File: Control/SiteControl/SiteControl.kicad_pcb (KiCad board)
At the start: 2 copper layers, 109.2 x 48.3 mm, 149 parts, among them J1 RJ50, J2 CONN_01X03, J3 IDC_16Pin_Polarized, J4 CONN_01X06, J5 IDC-10_Polarized, J6 CONN_01X02, P1 Molex Minifit-JR 4.2mm, Q1 BC817-40, Q2 SI2323DDS-T1-GE3, U1 Opto_H11L1M, U10 LMV611, U11 MAX17552, U12 ICL3221, U13 Opto_H11L1M, U14 Opto_H11L1M, U15 12-Bit SPI ADC, U16 MCP7952, U17 74HCT125D,653, U18 SN74AUP1T87_Schmitt_XNOR, U2 Opto_H11L1M, U3 Opto_H11L1M, U4 Opto_H11L1M, U5 Opto_H11L1M, U6 PIC16LF1947, U7 SS_Relay_VO14642AT, U8 SS_Relay_VO14642AT, U9 LM43602, X1 CFS-20632768EZBB_32.768kHz, Y1 4MHz

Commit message: [Added] indicator LEDs and a new 3V3 Buck Converter to Site Control Board
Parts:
- removed the ? at (174.7, 98.6)
- removed the ? at (174.7, 100.0)
- removed the ? at (176.8, 104.4)
- removed the ? at (167.0, 98.9)
- removed the ? at (171.7, 99.5)
- removed the ? at (169.4, 98.5)
- removed the ? at (171.2, 98.5)
- added C47: 18pF/25V, Capacitors_SMD:C_0805, B.Cu at (182.9, 102.0)
- added C48: 100uF, Capacitors_SMD:C_1210, B.Cu at (186.4, 87.0)
- added C49: 0.1uF, Capacitors_SMD:C_0603, B.Cu at (183.9, 87.8)
- added D2: Reverse Polarity Error, LEDs:LED_0805, F.Cu at (173.9, 124.5)
- added D3: BATT Power, LEDs:LED_0805, F.Cu at (180.3, 123.5)
- added D4: 3V3 Power, LEDs:LED_0805, F.Cu at (184.2, 84.6)
- added D5: 5V Power, LEDs:LED_0805, F.Cu at (179.8, 84.5)
- added D6: RPi VSENSE, LEDs:LED_0805, F.Cu at (188.2, 84.4)
- added D7: RTC_MFP, LEDs:LED_0805, F.Cu at (182.0, 84.5)
- added D8: MCU Active, LEDs:LED_0805, F.Cu at (186.4, 84.5)
- added D9: MCU Mode, LEDs:LED_0805, F.Cu at (177.7, 84.4)
- added R53: 750R, Resistors_SMD:R_0603, F.Cu at (181.9, 88.0)
- added R54: 750R, Resistors_SMD:R_0603, F.Cu at (186.1, 87.6)
- added R55: 750R, Resistors_SMD:R_0603, F.Cu at (177.9, 87.8)
- added R56: 205K, Resistors_SMD:R_0805, B.Cu at (197.8, 99.5)
- added R57: 1M, Resistors_SMD:R_0805, B.Cu at (182.9, 100.0)
- added R58: 442K, Resistors_SMD:R_0805, B.Cu at (186.3, 102.0)
- C22: value 1uF/100V -> 47uF; footprint Capacitors_SMD:C_1206 -> Capacitors_SMD:c_elec_4x5.8
- C23: value 0.22uF -> 1uF; footprint Capacitors_SMD:C_0603 -> Capacitors_SMD:C_0805
- C24: value 10uF/6.3V -> 4.7uF; footprint Capacitors_SMD:C_1206 -> Capacitors_SMD:C_1210
- C25: value 0.47uF -> 2.2uF; footprint Capacitors_SMD:C_0603 -> Capacitors_SMD:C_0805
- C26: value 0.1uF -> 0.47uF; footprint Capacitors_SMD:C_0603 -> Capacitors_SMD:C_0805
- C36: value 0.47uF/50V -> 4.7uF; footprint Capacitors_SMD:C_0603 -> Capacitors_SMD:C_0805; moved to F.Cu
- C38, C41, C42, C43, C44, C45, C46, D1, R25, R26, R43, R49, R50, U15, U16, U17, U18: moved to B.Cu
- L2: value 150uH -> 22uH; footprint DigitalLogic:SRR7045-151M_Inductor -> Inductors:SELF-WE-PD-XXL; moved to B.Cu
- R32: value 191K -> 3K6; moved to F.Cu
- R33: value 49K9 -> 5K6; moved to F.Cu
- R34: value 158K -> 750R; moved to F.Cu
- R35: value 22R1 -> 1K6; moved to F.Cu
- R36: value 1K -> 750R; moved to F.Cu
- U11: value MAX17552 -> LM43602; footprint DigitalLogic:MAX17552 -> DigitalLogic:TI_HTSSOP-PWP-16
- moved C21 140.4 mm to (180.9, 150.2), turned to 90 degrees
- moved C18 134.1 mm to (177.6, 142.5), turned to 90 degrees
- moved R27 126.5 mm to (194.3, 138.0), turned to 180 degrees
- moved P1 125.2 mm to (153.4, 132.0)
- moved C37 124.7 mm to (194.9, 142.5), turned to 180 degrees
- moved R29 123.7 mm to (182.8, 136.0)
- moved R28 121.3 mm to (179.0, 138.0)
- moved C16 120.2 mm to (173.4, 142.3), turned to 90 degrees
- moved C38 119.5 mm to (193.9, 139.0), turned to 270 degrees
- moved C17 119.4 mm to (180.4, 142.0), turned to 90 degrees
- moved L1 119.1 mm to (191.4, 150.0), turned to 270 degrees
- moved C19 114.8 mm to (194.4, 140.0), turned to 180 degrees
- moved C20 106.2 mm to (183.4, 150.0), turned to 90 degrees
- moved C39 105.9 mm to (179.1, 136.0), turned to 180 degrees
- moved R25 103.3 mm to (192.1, 137.0), turned to 180 degrees
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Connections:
- net Net-(Q2-Pad3) renamed I1
- C23 pad 1: Net-(C23-Pad1) -> GND
- C23 pad 2: GND -> +BATT
- C24 pad 1: +3V3 -> GND
- C24 pad 2: GND -> +BATT
- C25 pad 1: +3V3 -> GND
- C25 pad 2: GND -> Net-(C25-Pad2)
- C26 pad 1: +3V3 -> Net-(C26-Pad1)
- C26 pad 2: GND -> Net-(C26-Pad2)
- C36 pad 1: +BATT -> GND
- C36 pad 2: GND -> +3V3
- L2 pad 1: Net-(L2-Pad1) -> Net-(C26-Pad2)
- R26 pad 1: GND -> RPi_5v_PGood
- R26 pad 2: RPi_5v_PGood -> +3V3
- R32 pad 1: Net-(R32-Pad1) -> Net-(D2-Pad2)
- R33 pad 1: Net-(R33-Pad1) -> Net-(D3-Pad1)
- R34 pad 1: +3V3 -> Net-(D4-Pad1)
- R34 pad 2: Net-(R33-Pad1) -> GND
- R35 pad 1: +3V3 -> Net-(D5-Pad1)
- R35 pad 2: Net-(C23-Pad1) -> GND
- R36 pad 1: Net-(R36-Pad1) -> Net-(D6-Pad1)
- R36 pad 2: +3V3 -> GND
- U11 pad 1: +BATT -> Net-(C26-Pad2)
- U11 pad 10: Net-(L2-Pad1) -> GND
- U11 pad 2: +BATT -> Net-(C26-Pad2)
- U11 pad 3: Net-(R32-Pad1) -> Net-(C26-Pad1)
- U11 pad 4: Net-(U11-Pad4) -> Net-(C25-Pad2)
- U11 pad 5: Net-(R33-Pad1) -> +3V3
- U11 pad 6: Net-(C23-Pad1) -> GND
- U11 pad 7: Net-(R36-Pad1) -> Net-(R56-Pad2)
- U11 pad 9: GND -> Net-(C47-Pad1)
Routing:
- net +5V: track 0.00 -> 48.7 mm, vias 0 -> 3
- net +3V3: track 8.07 -> 54.2 mm, vias 1 -> 3
- net GND: track 17.8 -> 43.1 mm, vias 0 -> 2
- net RPi_5V_En: track 0.00 -> 14.1 mm, vias 0 -> 1
- net INV_TOGGLE: track 30.6 -> 43.7 mm
- net INV_LCD_GND: track 90.0 -> 102.5 mm, vias 4 -> 6
- net INV_LED_PowerOn: track 28.0 -> 18.6 mm
- net INV_LCD_Data: track 24.6 -> 15.6 mm
- net INV_LED_OverTemp: track 35.4 -> 44.1 mm
- net RPi_5v_PGood: track 0.00 -> 8.61 mm, vias 0 -> 1
- net Net-(C39-Pad1): track 0.00 -> 7.54 mm
- net Net-(C37-Pad1): track 0.00 -> 7.10 mm
- net Net-(C26-Pad1): track 0.00 -> 7.03 mm
- net Net-(C47-Pad1): track 0.00 -> 6.58 mm
- net Net-(R56-Pad2): track 0.00 -> 3.94 mm
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- added copper zone on F.Cu, net +5V
- added copper zone on F.Cu, net +BATT
- added copper zone on F.Cu, net GND
- added copper zone on B.Cu, net Net-(C26-Pad2)
- added copper zone on F.Cu, net Net-(C37-Pad2)
- removed copper zone on F.Cu, net +3V3
- removed copper zone on B.Cu, net Net-(L2-Pad1)
- removed copper zone on F.Cu, net Net-(L2-Pad1)
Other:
- board size 109.2 x 48.3 mm -> 52.5 x 115.5 mm

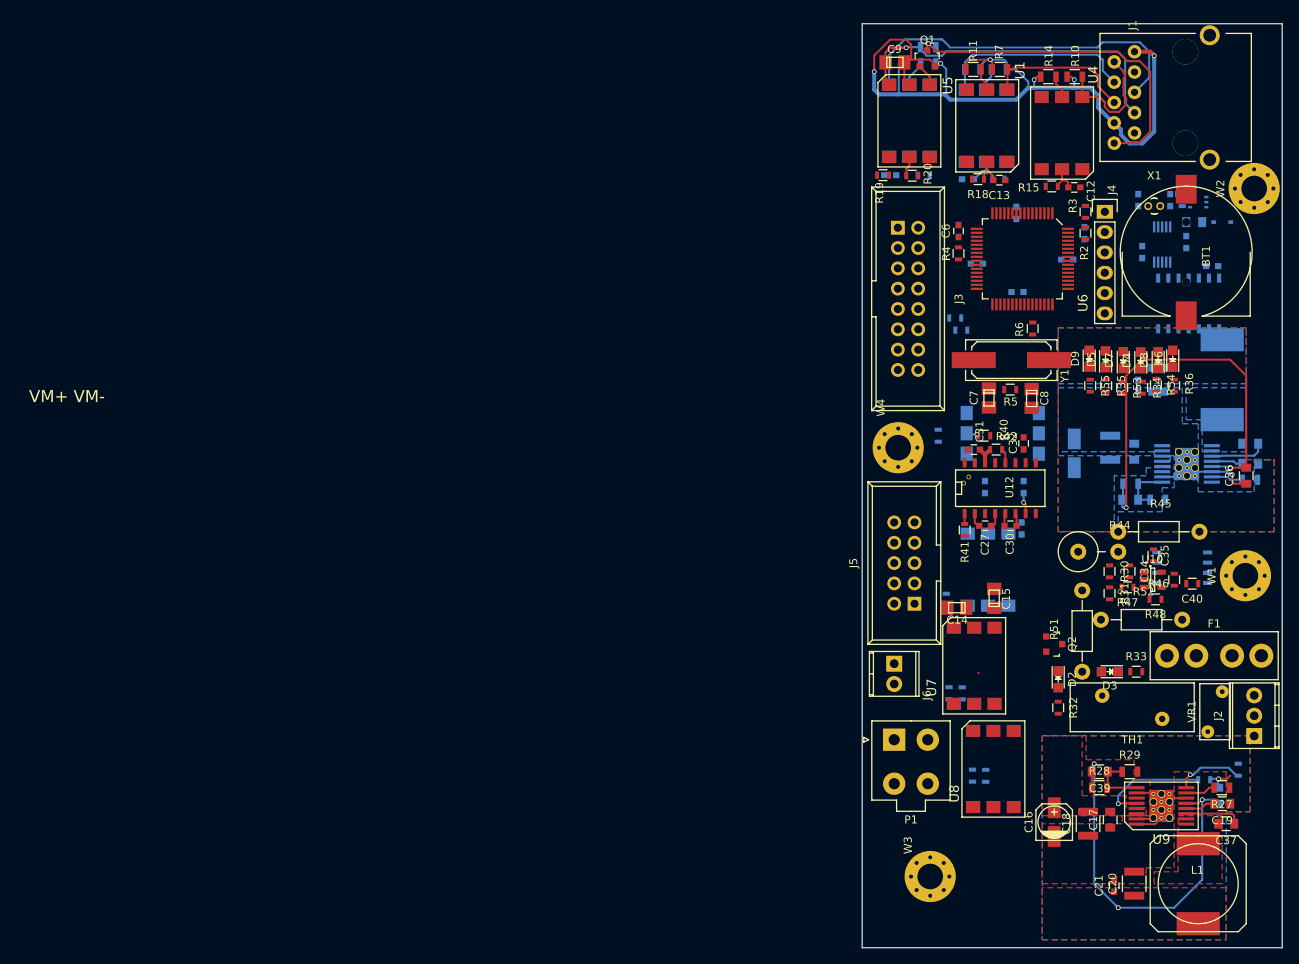
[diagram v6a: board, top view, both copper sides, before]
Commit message: [WIP] Preliminary routing and silkscreen placement for Rev B of Site Control Board Compelte
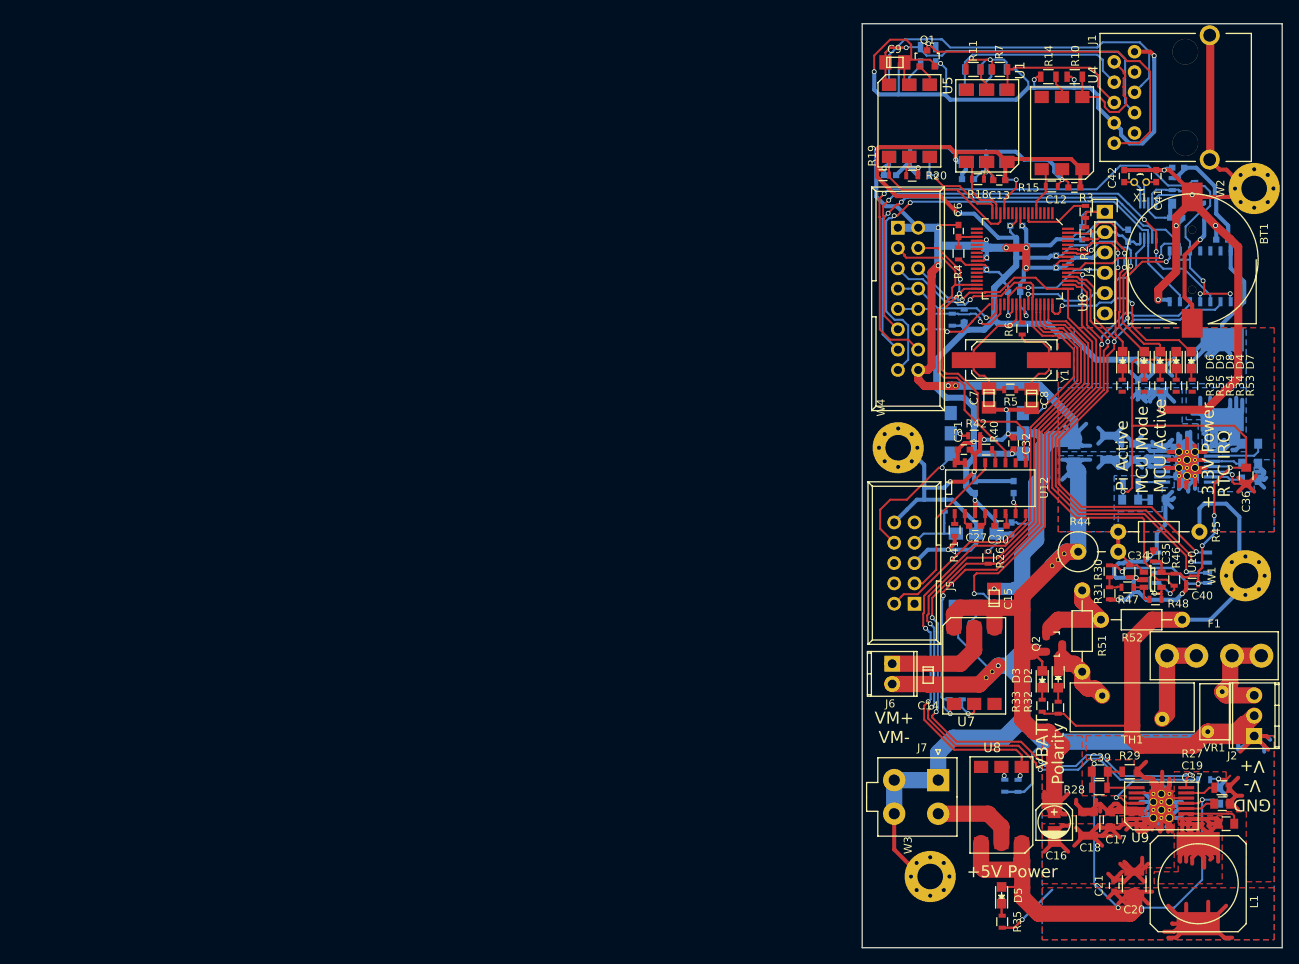
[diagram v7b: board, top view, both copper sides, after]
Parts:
- removed the ? at (162.7, 99.2)
- removed the ? at (162.0, 99.9)
- removed the ? at (181.6, 113.5)
- added ?: , DigitalLogic:Via, F.Cu at (161.0, 87.8)
- added ?: , DigitalLogic:Via, F.Cu at (164.9, 124.2)
- added ?: , DigitalLogic:Via, F.Cu at (165.6, 123.5)
- added ?: , DigitalLogic:Via, F.Cu at (173.1, 110.2)
- added ?: , DigitalLogic:Via, F.Cu at (173.9, 109.5)
- added ?: , DigitalLogic:Via, F.Cu at (174.6, 108.8)
- C41, C42, R26: moved to F.Cu
- moved R35 68.2 mm to (166.9, 154.8)
- moved D5 68.2 mm to (166.8, 151.5)
- moved R26 41.0 mm to (165.1, 109.2)
- moved R33 12.5 mm to (171.9, 127.8), turned to 270 degrees
- moved C14 9.15 mm to (157.6, 123.9), turned to 90 degrees
- moved R39 8.78 mm to (159.6, 102.8), turned to 90 degrees
- moved R53 8.75 mm to (190.6, 87.8)
- moved D3 8.50 mm to (171.9, 124.5), turned to 90 degrees
- moved D7 8.50 mm to (190.5, 84.5)
- moved J7 7.47 mm to (158.9, 137.1), turned to 270 degrees
- moved D9 6.88 mm to (184.6, 84.5)
- moved R55 6.75 mm to (184.6, 87.8)
- moved R36 6.50 mm to (181.9, 87.8)
- moved D6 6.25 mm to (181.9, 84.5)
- moved R24 5.83 mm to (168.8, 137.8), turned to 90 degrees
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- renumbered P1 to J7
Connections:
- D6 pad 2: Pi_VSense -> Pi_Sense
- J3 pad 5: CMOS_RTS -> CMOS_CTS
- J3 pad 6: CMOS_CTS -> CMOS_RTS
- R26 pad 1: RPi_5v_PGood -> RPi_5V_PGood
- U6 pad 13: INV_Power_Safe -> INV_Overload_Safe
- U6 pad 15: INV_Overload_Safe -> INV_Temp_Safe
- U6 pad 16: INV_Temp_Safe -> INV_Power_Safe
- U6 pad 31: Modem_En -> CMOS_TX
- U6 pad 32: INV_Data_Safe -> CMOS_RX
- U6 pad 4: CMOS_TX -> Net-(U6-Pad4)
- U6 pad 43: RPi_5V_En -> CMOS_CTS
- U6 pad 44: CMOS_RTS -> RPi_En
- U6 pad 45: Net-(U6-Pad45) -> RPi_5V_En
- U6 pad 46: CMOS_CTS -> RPi_5V_PGood
- U6 pad 47: RPi_En -> Modem_En
- U6 pad 49: Net-(U6-Pad49) -> CMOS_RTS
- U6 pad 5: CMOS_RX -> INV_Data_Safe
- U6 pad 58: Net-(U6-Pad58) -> MCU_Active
- U6 pad 59: Net-(U6-Pad59) -> Pi_Sense
- U6 pad 63: Net-(U6-Pad63) -> MCU_Mode
- U8 pad 5: Net-(P1-Pad2) -> Net-(J7-Pad2)
- U9 pad 8: RPi_5v_PGood -> RPi_5V_PGood
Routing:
- net GND: track 43.1 -> 942.6 mm, vias 2 -> 34
- net +3V3: track 54.2 -> 351.9 mm, vias 3 -> 18
- net +BATT: track 0.00 -> 128.9 mm
- net RPi_5V_PGood: track 0.00 -> 104.9 mm, vias 0 -> 4
- net RPi_5V_En: track 14.1 -> 110.7 mm, vias 1 -> 4
- net RPi_En: track 0.00 -> 84.7 mm, vias 0 -> 3
- net +5V: track 48.7 -> 130.4 mm
- net CMOS_RTS: track 0.00 -> 73.2 mm, vias 0 -> 2
- net SDI: track 0.00 -> 71.2 mm, vias 0 -> 4
- net SDO: track 0.00 -> 70.1 mm, vias 0 -> 2
- net SCLK: track 0.00 -> 69.8 mm, vias 0 -> 2
- net PI_SDO: track 0.00 -> 68.0 mm, vias 0 -> 3
- net Modem_En: track 0.00 -> 66.9 mm, vias 0 -> 2
- net PI_SCLK: track 0.00 -> 66.7 mm, vias 0 -> 2
- net PI_RTC_nCS: track 0.00 -> 64.8 mm, vias 0 -> 1
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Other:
- board text added: "+3.3V Power"
- board text added: "+5V Power"
- board text added: "Applied Physics Club PSU Array Site Control Rev B The Pennsylvania State University"
- board text added: "MCU Active"
- board text added: "MCU Mode"
- board text added: "Pi Active"
- board text added: "Polarity"
- board text added: "RTC IRQ"
- board text added: "VBATT"
- board text removed: "Applied Physics Club PSU Array Site Control Rev 1.0 The Pennsylvania State University"
